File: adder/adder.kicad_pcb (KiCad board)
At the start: 2 copper layers, 1 part, among them U1 mini-vertical-slide-switch

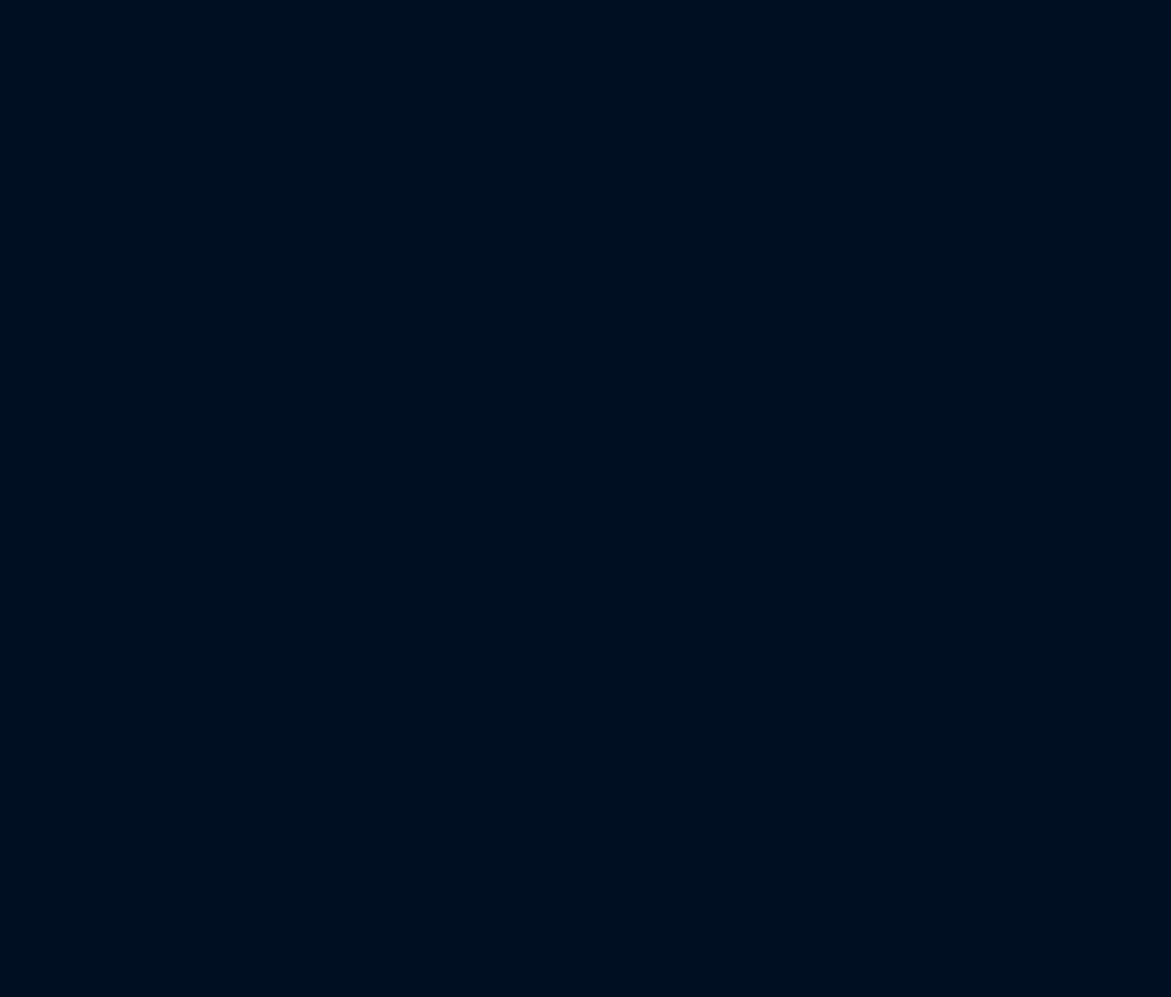
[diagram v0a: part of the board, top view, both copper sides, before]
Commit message: First (incomplete) version of a 4-bit adder
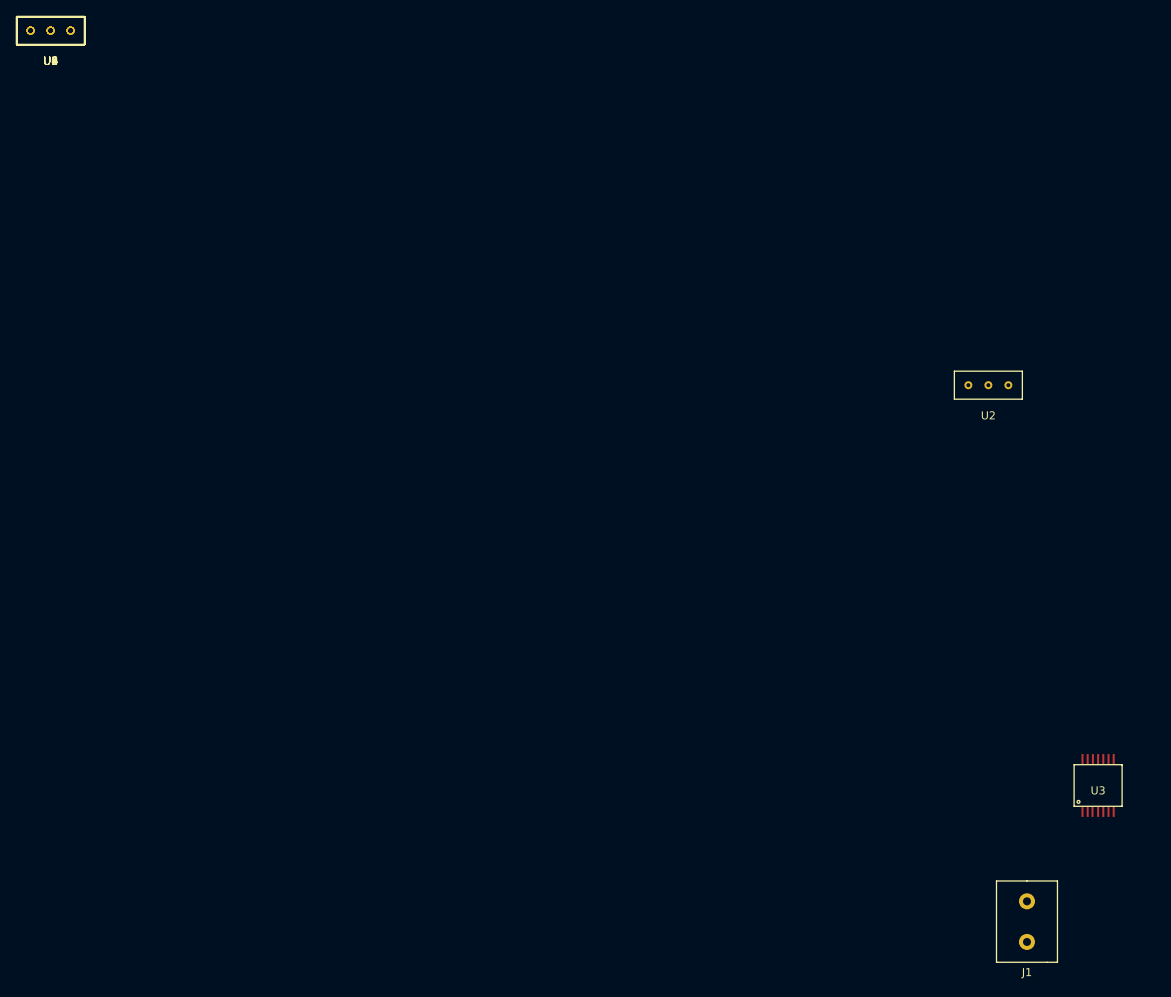
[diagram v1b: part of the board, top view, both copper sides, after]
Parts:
- added J1: CONN_01X02, library:screw-terminal-01x02, F.Cu at (122.0, 111.4)
- added U2: mini-vertical-slide-switch, library:mini-vertical-slide-switch, F.Cu at (117.2, 44.3)
- added U3: 74LS136, library:ssop14, F.Cu at (130.9, 94.4)
- added U4, U5, U6, U7, U8, U9: mini-vertical-slide-switch, library:mini-vertical-slide-switch, F.Cu at (0.00, 0.00)
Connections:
- U1 pad 1: Net-(U1-Pad1) -> VCC

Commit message: Finished diagram and started on pcb layout hell
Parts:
- added D1: S1, LEDs:LED_0805_HandSoldering, F.Cu at (113.0, 107.3)
- added D10: LB4, LEDs:LED_0805_HandSoldering, F.Cu at (135.3, 84.5)
- added D11: A4, LEDs:LED_0805_HandSoldering, F.Cu at (117.5, 84.5)
- added D12: S4, LEDs:LED_0805_HandSoldering, F.Cu at (131.4, 107.3)
- added D2: LB1, LEDs:LED_0805_HandSoldering, F.Cu at (123.8, 84.5)
- added D3: LA1, LEDs:LED_0805_HandSoldering, F.Cu at (106.0, 84.5)
- added D4: S2, LEDs:LED_0805_HandSoldering, F.Cu at (118.7, 107.3)
- added D5: LB2, LEDs:LED_0805_HandSoldering, F.Cu at (127.6, 84.5)
- added D6: LA2, LEDs:LED_0805_HandSoldering, F.Cu at (109.9, 84.5)
- added D7: LB3, LEDs:LED_0805_HandSoldering, F.Cu at (131.4, 84.5)
- added D8: LA3, LEDs:LED_0805_HandSoldering, F.Cu at (113.7, 84.5)
- added D9: S3, LEDs:LED_0805_HandSoldering, F.Cu at (125.1, 107.3)
- added J2: B, Pin_Headers:Pin_Header_Straight_1x04_Pitch2.54mm, F.Cu at (133.3, 71.1)
- added J3: A, Pin_Headers:Pin_Header_Straight_1x04_Pitch2.54mm, F.Cu at (108.0, 71.1)
- added J4: VOUT, Pin_Headers:Pin_Header_Straight_1x03_Pitch2.54mm, F.Cu at (86.4, 91.4)
- added U10: XOR, library:ssop14, B.Cu at (114.3, 94.0)
- added U11: AND, library:ssop14, B.Cu at (107.3, 94.0)
- added U12: A4, library:mini-vertical-slide-switch, F.Cu at (117.5, 77.5)
- added U13: B4, library:mini-vertical-slide-switch, F.Cu at (135.3, 77.5)
- J1: value CONN_01X02 -> VIN; footprint library:screw-terminal-01x02 -> Pin_Headers:Pin_Header_Straight_1x03_Pitch2.54mm
- U1: value mini-vertical-slide-switch -> XOR; footprint library:mini-vertical-slide-switch -> library:ssop14; moved to B.Cu
- U2: value mini-vertical-slide-switch -> AND; footprint library:mini-vertical-slide-switch -> library:ssop14; moved to B.Cu
- U3: value 74LS136 -> A1; footprint library:ssop14 -> library:mini-vertical-slide-switch
- U4: value mini-vertical-slide-switch -> B1
- U5: value mini-vertical-slide-switch -> A2
- U6: value mini-vertical-slide-switch -> B2
- U7: value mini-vertical-slide-switch -> OR; footprint library:mini-vertical-slide-switch -> library:ssop14; moved to B.Cu
- U8: value mini-vertical-slide-switch -> A3
- U9: value mini-vertical-slide-switch -> B3
- moved U7 153.4 mm to (121.3, 94.0)
- moved U9 152.6 mm to (131.4, 77.5), turned to 90 degrees
- moved U6 149.3 mm to (127.6, 77.5), turned to 90 degrees
- moved U4 146.1 mm to (123.8, 77.5), turned to 90 degrees
- moved U8 137.6 mm to (113.7, 77.5), turned to 90 degrees
- moved U5 134.4 mm to (109.9, 77.5), turned to 90 degrees
- moved U2 52.8 mm to (135.3, 94.0)
- moved J1 37.6 mm to (153.0, 90.2)
- moved U3 30.1 mm to (106.0, 77.5), turned to 90 degrees
- moved U1 23.0 mm to (128.3, 94.0)
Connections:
- J1 pad 1: GND -> VCC
- J1 pad 2: VCC -> GND
- U1 pad 1: VCC -> /A1
- U1 pad 2: Net-(U1-Pad2) -> /B1
- U1 pad 3: Net-(U1-Pad3) -> /XI1
- U2 pad 1: VCC -> /XI1
- U2 pad 2: Net-(U2-Pad2) -> /CIN
- U2 pad 3: Net-(U2-Pad3) -> /CX1
- U3 pad 1: Net-(U2-Pad3) -> VCC
- U3 pad 2: Net-(U3-Pad2) -> (no net)
- U3 pad 3: GND -> /A1
- U4 pad 2: Net-(U3-Pad5) -> (no net)
- U4 pad 3: Net-(U3-Pad4) -> /B1
- U5 pad 2: Net-(U3-Pad13) -> (no net)
- U5 pad 3: Net-(U3-Pad12) -> /A2
- U6 pad 2: Net-(U6-Pad2) -> (no net)
- U6 pad 3: Net-(U6-Pad3) -> /B2
- U7 pad 1: VCC -> /AI2
- U7 pad 2: Net-(U7-Pad2) -> /CX2
- U7 pad 3: Net-(U7-Pad3) -> /C2
- U8 pad 2: Net-(U8-Pad2) -> (no net)
- U8 pad 3: Net-(U8-Pad3) -> /A3
- U9 pad 2: Net-(U9-Pad2) -> (no net)
- U9 pad 3: Net-(U9-Pad3) -> /B3
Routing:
- net /C3: track 0.00 -> 22.8 mm, vias 0 -> 4
- net /CX3: track 0.00 -> 22.5 mm
- net /C2: track 0.00 -> 22.1 mm, vias 0 -> 2
- net /CX4: track 0.00 -> 22.0 mm
- net /AI3: track 0.00 -> 20.0 mm, vias 0 -> 2
- net /AI4: track 0.00 -> 15.6 mm, vias 0 -> 2
- net /XI3: track 0.00 -> 15.3 mm
- net /XI4: track 0.00 -> 13.1 mm
- net /A4: track 0.00 -> 12.4 mm
- net /B4: track 0.00 -> 11.1 mm, vias 0 -> 2
- net /A3: track 0.00 -> 9.08 mm
- net /B3: track 0.00 -> 7.39 mm, vias 0 -> 2
- added copper zone on F.Cu, net GND
- added copper zone on B.Cu, net VCC
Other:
- net class Default: clearance 0.2 -> 0.125
- rule trace_clearance: 0.2 -> 0.125

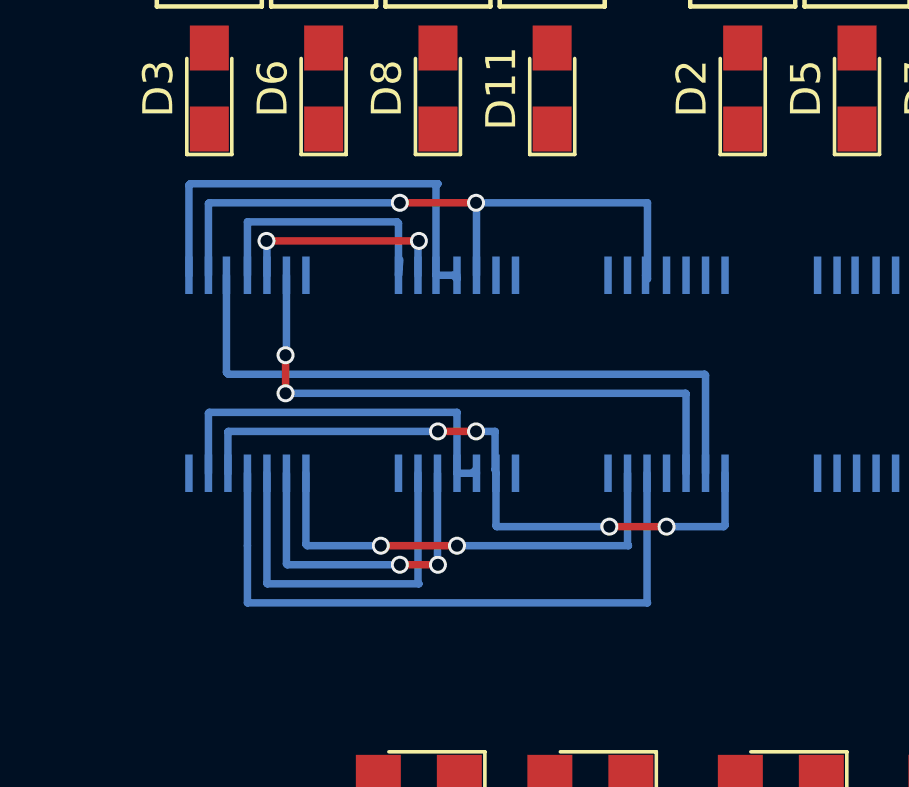
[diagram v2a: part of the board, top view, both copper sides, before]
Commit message: Updated traces to match OshPark's
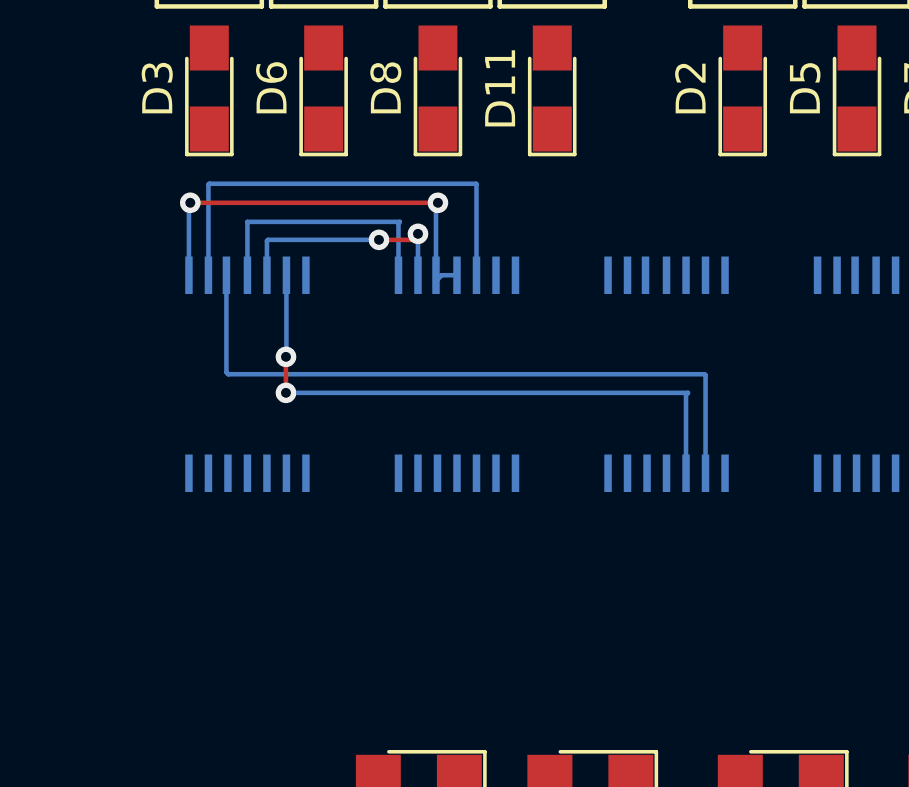
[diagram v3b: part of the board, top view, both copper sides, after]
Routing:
- net /C3: track 22.8 -> 0.00 mm, vias 4 -> 0
- net /CX4: track 22.0 -> 0.00 mm
- net /AI4: track 15.6 -> 0.00 mm, vias 2 -> 0
- net /XI4: track 13.1 -> 0.00 mm
- net /A4: track 12.4 -> 0.00 mm
- net /B4: track 11.1 -> 0.00 mm, vias 2 -> 0
- net /C2: track 22.1 -> 15.0 mm, vias 2 -> 0
- net /XI3: track 15.3 -> 14.0 mm, vias 0 -> 2
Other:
- net class Default: clearance 0.125 -> 0.1524; trace_width 0.25 -> 0.1524; via_dia 0.6 -> 0.6858; via_drill 0.4 -> 0.3302
- rule trace_clearance: 0.125 -> 0.1524
- rule trace_min: 0.2 -> 0.1524
- rule via_min_drill: 0.3 -> 0.3302
- rule via_min_size: 0.4 -> 0.6858

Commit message: Did some more work on the PCB design hell
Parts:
- moved J4 53.6 mm to (139.7, 96.8), turned to 180 degrees
- moved J1 50.5 mm to (102.9, 96.6), turned to 180 degrees
- moved D12 10.8 mm to (130.8, 96.5), turned to 0 degrees
- moved D4 10.8 mm to (119.8, 96.6), turned to 0 degrees
- moved D1 10.8 mm to (113.9, 96.6), turned to 0 degrees
- moved D9 10.7 mm to (125.4, 96.6), turned to 0 degrees
- moved J2 8.44 mm to (135.0, 79.4)
- moved U4 8.37 mm to (125.8, 85.6)
- moved U6 8.34 mm to (129.5, 85.6)
- moved U9 8.30 mm to (133.1, 85.6)
- moved U13 8.28 mm to (136.8, 85.6)
- moved D2 8.19 mm to (125.8, 92.4)
- moved D5 8.16 mm to (129.5, 92.4)
- moved D7 8.12 mm to (133.1, 92.4)
- moved J3 8.09 mm to (107.5, 79.2)
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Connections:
- U12 pad 2: (no net) -> Net-(U12-Pad2)
- U13 pad 2: (no net) -> Net-(U13-Pad2)
- U3 pad 2: (no net) -> Net-(U3-Pad2)
- U4 pad 2: (no net) -> Net-(U4-Pad2)
- U5 pad 2: (no net) -> Net-(U5-Pad2)
- U6 pad 2: (no net) -> Net-(U6-Pad2)
- U8 pad 2: (no net) -> Net-(U8-Pad2)
- U9 pad 2: (no net) -> Net-(U9-Pad2)
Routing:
- net /A1: track 0.00 -> 57.5 mm, vias 0 -> 4
- net /A2: track 0.00 -> 48.3 mm, vias 0 -> 2
- net /B3: track 7.66 -> 40.4 mm, vias 2 -> 4
- net /A3: track 8.66 -> 27.2 mm, vias 0 -> 4
- net /CX3: track 22.5 -> 35.5 mm
- net /A4: track 0.00 -> 12.3 mm
- net /C2: track 15.0 -> 24.9 mm, vias 0 -> 2
- net /XI3: track 14.0 -> 20.7 mm, vias 2 -> 0
- net VCC: track 0.00 -> 3.10 mm
- net GND: track 0.00 -> 3.07 mm, vias 0 -> 1
- net /AI3: track 20.0 -> 19.9 mm, vias 2 -> 0
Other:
- board outline added: 41.3 x 21.8 mm

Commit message: Finished v2 of adder
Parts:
- removed D1: S1, LEDs:LED_0805_HandSoldering
- removed D10: LB4, LEDs:LED_0805_HandSoldering
- removed D11: A4, LEDs:LED_0805_HandSoldering
- removed D12: S4, LEDs:LED_0805_HandSoldering
- removed D2: LB1, LEDs:LED_0805_HandSoldering
- removed D3: LA1, LEDs:LED_0805_HandSoldering
- removed D4: S2, LEDs:LED_0805_HandSoldering
- removed D5: LB2, LEDs:LED_0805_HandSoldering
- removed D6: LA2, LEDs:LED_0805_HandSoldering
- removed D7: LB3, LEDs:LED_0805_HandSoldering
- removed D8: LA3, LEDs:LED_0805_HandSoldering
- removed D9: S3, LEDs:LED_0805_HandSoldering
- removed J1: VIN, Pin_Headers:Pin_Header_Straight_1x03_Pitch2.54mm
- removed J2: B, Pin_Headers:Pin_Header_Straight_1x04_Pitch2.54mm
- removed J3: A, Pin_Headers:Pin_Header_Straight_1x04_Pitch2.54mm
- removed J4: VOUT, Pin_Headers:Pin_Header_Straight_1x03_Pitch2.54mm
- removed U1, U10: XOR, library:ssop14
- removed U11, U2: AND, library:ssop14
- removed U12: A4, library:mini-vertical-slide-switch
- removed U13: B4, library:mini-vertical-slide-switch
- removed U3: A1, library:mini-vertical-slide-switch
- removed U4: B1, library:mini-vertical-slide-switch
- removed U5: A2, library:mini-vertical-slide-switch
- removed U6: B2, library:mini-vertical-slide-switch
- removed U7: OR, library:ssop14
- removed U8: A3, library:mini-vertical-slide-switch
- removed U9: B3, library:mini-vertical-slide-switch
- added A1: LA1, LEDs:LED_0805_HandSoldering, F.Cu at (136.2, 109.3)
- added A1: A1, library:mini-vertical-slide-switch, F.Cu at (136.2, 104.0)
- added A2: LA2, LEDs:LED_0805_HandSoldering, F.Cu at (141.2, 109.3)
- added A2: A2, library:mini-vertical-slide-switch, F.Cu at (141.2, 104.0)
- added A3: LA3, LEDs:LED_0805_HandSoldering, F.Cu at (146.2, 109.3)
- added A3: A3, library:mini-vertical-slide-switch, F.Cu at (146.1, 104.0)
- added A4: A4, LEDs:LED_0805_HandSoldering, F.Cu at (151.1, 109.2)
- added A4: A4, library:mini-vertical-slide-switch, F.Cu at (151.1, 104.0)
- added AND: AND, library:ssop14, B.Cu at (147.2, 115.3)
- added AND: AND, library:ssop14, B.Cu at (165.3, 115.3)
- added B1: LB1, LEDs:LED_0805_HandSoldering, F.Cu at (161.2, 109.3)
- added B1: B1, library:mini-vertical-slide-switch, F.Cu at (161.2, 104.0)
- added B2: LB2, LEDs:LED_0805_HandSoldering, F.Cu at (166.4, 109.3)
- added B2: B2, library:mini-vertical-slide-switch, F.Cu at (166.4, 104.0)
- added B3: LB3, LEDs:LED_0805_HandSoldering, F.Cu at (171.3, 109.3)
- added B3: B3, library:mini-vertical-slide-switch, F.Cu at (171.3, 104.0)
- added B4: LB4, LEDs:LED_0805_HandSoldering, F.Cu at (176.2, 109.3)
- added B4: B4, library:mini-vertical-slide-switch, F.Cu at (176.1, 104.0)
- added CIN: VIN, Pin_Headers:Pin_Header_Straight_1x03_Pitch2.54mm, F.Cu at (131.7, 113.0)
- added COUT: VOUT, Pin_Headers:Pin_Header_Straight_1x03_Pitch2.54mm, F.Cu at (180.8, 113.0)
- added OR: OR, library:ssop14, B.Cu at (156.3, 115.3)
- added S1: S1, LEDs:LED_0805_HandSoldering, F.Cu at (142.7, 115.4)
- added S2: S2, LEDs:LED_0805_HandSoldering, F.Cu at (151.6, 115.2)
- added S3: S3, LEDs:LED_0805_HandSoldering, F.Cu at (160.7, 115.1)
- added S4: S4, LEDs:LED_0805_HandSoldering, F.Cu at (169.8, 115.1)
- added VIN: A, Pin_Headers:Pin_Header_Straight_1x04_Pitch2.54mm, F.Cu at (131.7, 109.3)
- added VOUT: B, Pin_Headers:Pin_Header_Straight_1x04_Pitch2.54mm, F.Cu at (180.8, 109.3)
- added XOR: XOR, library:ssop14, B.Cu at (138.1, 115.3)
- added XOR: XOR, library:ssop14, B.Cu at (174.3, 115.3)
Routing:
- net VCC: track 3.10 -> 132.8 mm, vias 0 -> 1
- net GND: track 3.07 -> 115.3 mm, vias 1 -> 2
- net /A4: track 12.3 -> 95.4 mm
- net /B2: track 0.00 -> 62.3 mm, vias 0 -> 2
- net /B1: track 0.00 -> 59.9 mm
- net /B4: track 0.00 -> 44.5 mm
- net /COUT: track 0.00 -> 31.2 mm
- net /A1: track 57.5 -> 26.5 mm, vias 4 -> 0
- net /C1: track 0.00 -> 29.5 mm
- net /C3: track 0.00 -> 27.7 mm
- net /A3: track 27.2 -> 51.4 mm, vias 4 -> 1
- net /CIN: track 0.00 -> 22.0 mm
- net /AI4: track 0.00 -> 21.5 mm
- net /S3: track 0.00 -> 20.9 mm, vias 0 -> 1
- net /CX1: track 0.00 -> 20.5 mm
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- removed copper zone on F.Cu, net GND
- removed copper zone on B.Cu, net VCC
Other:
- board size 41.3 x 21.8 mm -> 52.9 x 21.5 mm
- board text added: "CIN"
- board text added: "COUT"
- board text added: "GND"
- board text added: "VCC"
